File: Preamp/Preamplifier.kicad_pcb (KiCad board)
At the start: 2 copper layers, 100 x 52 mm, 148 parts, among them J1 Conn_01x03_Male, J12 XLR3, J14 Conn_01x03, J15 Conn_01x02, J16 Conn_01x02, J17 Conn_01x02, J2 Conn_01x02_Male, J3 Conn_01x02_Male, J4 Conn_01x03_Male, J5 Conn_01x03_Male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

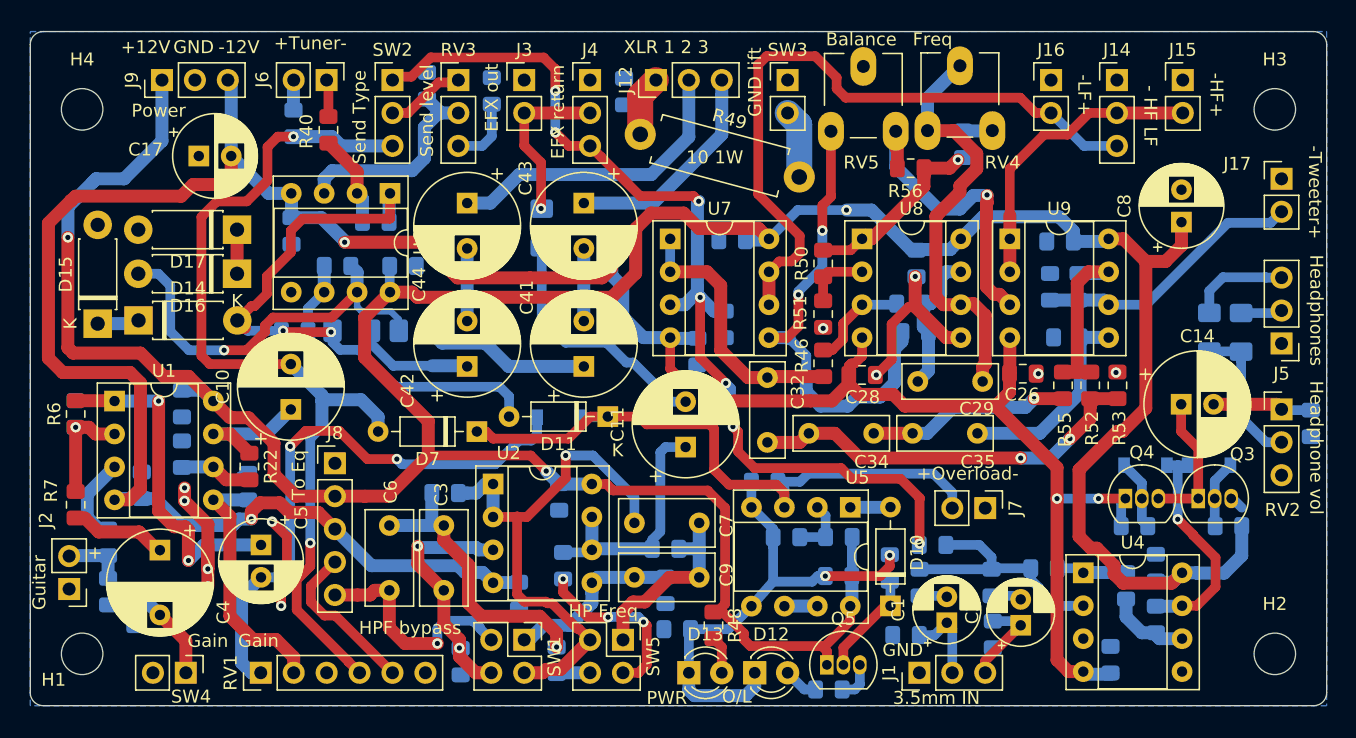
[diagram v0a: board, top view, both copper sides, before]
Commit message: Added top-side ground plane, started power supply work
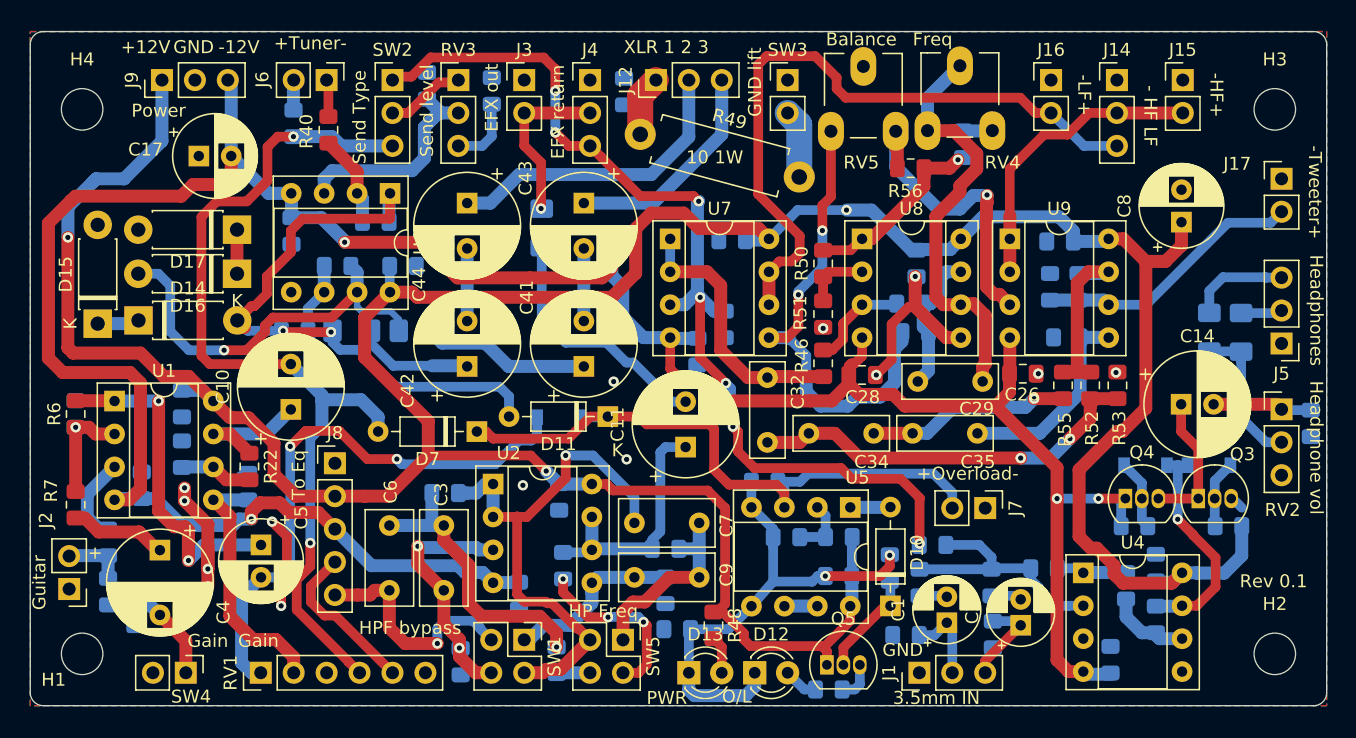
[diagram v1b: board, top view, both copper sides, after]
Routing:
- net GND: vias 11 -> 14
- added copper zone on F.Cu, net GND
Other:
- board text added: "Rev 0.1"
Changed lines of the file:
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@@
   (general
     (thickness 1.6)
-    (drawings 42)
-    (tracks 937)
+    (drawings 43)
+    (tracks 940)
     (zones 0)
     (modules 148)
@@
   )
   (setup
-    (last_trace_width 1)
+    (last_trace_width 0.25)
     (user_trace_width 0.5)
     (user_trace_width 0.75)
@@
     )
   )
+  (gr_text "Rev 0.1" (at 95.9 90.4) (layer F.SilkS)
+    (effects (font (size 1 1) (thickness 0.15)))
+  )
   (gr_text +Overload- (at 72.3 82.1) (layer F.SilkS)
     (effects (font (size 1 1) (thickness 0.25)))
@@
   (segment (start 67.78863 69.22137) (end 68.26 69.22137) (width 0.75) (layer F.Cu) (net 19))
   (segment (start 66.44 70.57) (end 67.78863 69.22137) (width 0.75) (layer F.Cu) (net 19))
+  (via (at 45 75) (size 0.8) (drill 0.4) (layers F.Cu B.Cu) (net 19))
+  (via (at 46 81) (size 0.8) (drill 0.4) (layers F.Cu B.Cu) (net 19))
+  (via (at 38 83) (size 0.8) (drill 0.4) (layers F.Cu B.Cu) (net 19))
   (via (at 62.96 61.77) (size 0.8) (drill 0.4) (layers F.Cu B.Cu) (net 20))
   (segment (start 56.88 64.09) (end 56.98 63.99) (width 1) (layer B.Cu) (net 20) (status 30))
@@
     (fill yes (arc_segments 32) (thermal_gap 0.508) (thermal_bridge_width 0.508))
     (polygon
+      (pts
+        (xy 100 100) (xy 0 100) (xy 0 48) (xy 100 48)
+      )
+    )
+  )
+  (zone (net 19) (net_name GND) (layer F.Cu) (hatch edge 0.508)
+    (connect_pads (clearance 0.508))
+    (min_thickness 0.254)
+    (fill yes (arc_segments 32) (thermal_gap 0.508) (thermal_bridge_width 0.508))
+    (polygon
